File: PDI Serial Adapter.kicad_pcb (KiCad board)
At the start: 2 copper layers, 40 x 17.5 mm, 7 parts, among them J1 2.54, J2 1.27, J3 PROG, J4 FTDI, J5 FTDI_VCC, J6 DTR_RST, J7 TARGET_PWR

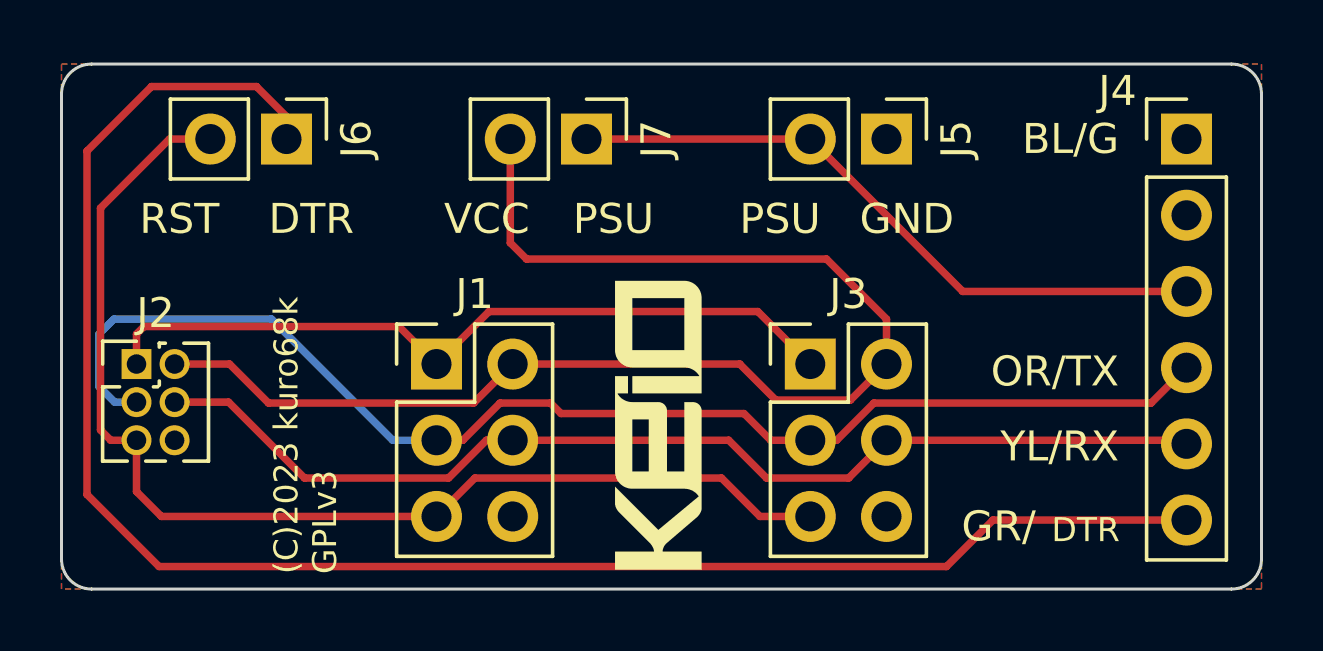
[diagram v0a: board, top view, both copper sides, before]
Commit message: Removed RX/TX from programmer header
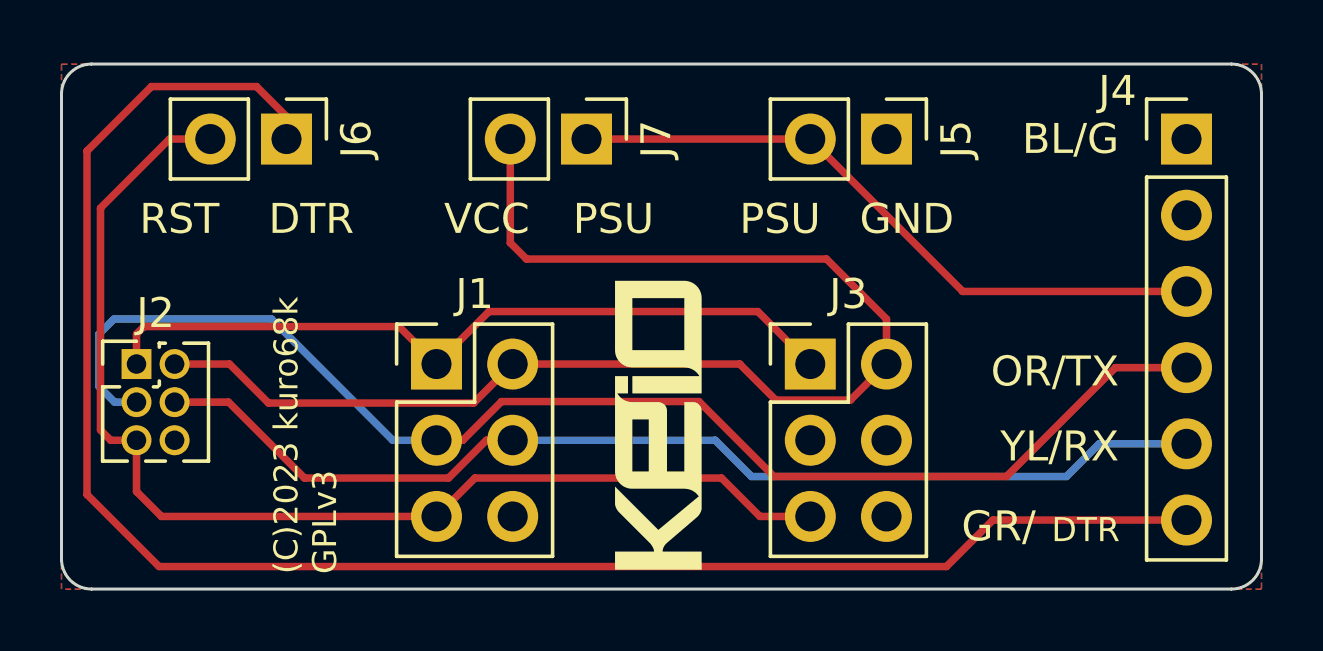
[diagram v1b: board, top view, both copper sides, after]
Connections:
- J3 pad 3: /MCU_RX -> unconnected-(J3-Pin_3-Pad3)
- J3 pad 4: /MCU_TX -> unconnected-(J3-Pin_4-Pad4)
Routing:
- net /MCU_RX: track 43.4 -> 44.4 mm
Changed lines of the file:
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@@
   (net 8 "/FTDI_VCC")
   (net 9 "/DTR")
+  (net 10 "unconnected-(J3-Pin_3-Pad3)")
+  (net 11 "unconnected-(J3-Pin_4-Pad4)")
   (footprint "Connector_PinHeader_2.54mm:PinHeader_2x03_P2.54mm_Vertical" (layer "F.Cu")
     (at 115 52.5)
@@
       (net 2 "/VCC") (pinfunction "Pin_2") (pintype "passive"))
     (pad "3" thru_hole oval (at 0 2.54) (size 1.7 1.7) (drill 1) (layers "*.Cu" "*.Mask")
-      (net 3 "/MCU_RX") (pinfunction "Pin_3") (pintype "passive"))
+      (net 10 "unconnected-(J3-Pin_3-Pad3)") (pinfunction "Pin_3") (pintype "passive+no_connect"))
     (pad "4" thru_hole oval (at 2.54 2.54) (size 1.7 1.7) (drill 1) (layers "*.Cu" "*.Mask")
-      (net 4 "/MCU_TX") (pinfunction "Pin_4") (pintype "passive"))
+      (net 11 "unconnected-(J3-Pin_4-Pad4)") (pinfunction "Pin_4") (pintype "passive+no_connect"))
     (pad "5" thru_hole oval (at 0 5.08) (size 1.7 1.7) (drill 1) (layers "*.Cu" "*.Mask")
       (net 5 "/PDI_CLK") (pinfunction "Pin_5") (pintype "passive"))
@@
   (segment (start 130 51) (end 128 49) (width 0.25) (layer "F.Cu") (net 2))
   (segment (start 128 49) (end 118 49) (width 0.25) (layer "F.Cu") (net 2))
-  (segment (start 127.46 55.04) (end 128.338299 55.04) (width 0.25) (layer "F.Cu") (net 3))
-  (segment (start 128.338299 55.04) (end 129.578299 53.8) (width 0.25) (layer "F.Cu") (net 3))
-  (segment (start 125.25 54.15) (end 126.14 55.04) (width 0.25) (layer "F.Cu") (net 3))
-  (segment (start 119.15 54.15) (end 125.25 54.15) (width 0.25) (layer "F.Cu") (net 3))
-  (segment (start 129.578299 53.8) (end 138.82 53.8) (width 0.25) (layer "F.Cu") (net 3))
-  (segment (start 126.14 55.04) (end 127.46 55.04) (width 0.25) (layer "F.Cu") (net 3))
-  (segment (start 115.878299 55.04) (end 117.118299 53.8) (width 0.25) (layer "F.Cu") (net 3))
   (segment (start 115 55.04) (end 115.878299 55.04) (width 0.25) (layer "F.Cu") (net 3))
-  (segment (start 117.118299 53.8) (end 118.8 53.8) (width 0.25) (layer "F.Cu") (net 3))
-  (segment (start 138.82 53.8) (end 140 52.62) (width 0.25) (layer "F.Cu") (net 3))
-  (segment (start 118.8 53.8) (end 119.15 54.15) (width 0.25) (layer "F.Cu") (net 3))
+  (segment (start 137.63 52.62) (end 140 52.62) (width 0.25) (layer "F.Cu") (net 3))
+  (segment (start 117.168299 53.75) (end 123.75 53.75) (width 0.25) (layer "F.Cu") (net 3))
+  (segment (start 123.75 53.75) (end 126.25 56.25) (width 0.25) (layer "F.Cu") (net 3))
+  (segment (start 126.25 56.25) (end 134 56.25) (width 0.25) (layer "F.Cu") (net 3))
+  (segment (start 134 56.25) (end 137.63 52.62) (width 0.25) (layer "F.Cu") (net 3))
+  (segment (start 115.878299 55.04) (end 117.168299 53.75) (width 0.25) (layer "F.Cu") (net 3))
   (segment (start 109.5 51) (end 113.54 55.04) (width 0.25) (layer "B.Cu") (net 3))
   (segment (start 104.25 51) (end 109.5 51) (width 0.25) (layer "B.Cu") (net 3))
@@
   (segment (start 113.54 55.04) (end 115 55.04) (width 0.25) (layer "B.Cu") (net 3))
   (segment (start 115.401701 56.3) (end 110.6 56.3) (width 0.25) (layer "F.Cu") (net 4))
-  (segment (start 124.74 55.04) (end 126 56.3) (width 0.25) (layer "F.Cu") (net 4))
-  (segment (start 117.54 55.04) (end 124.74 55.04) (width 0.25) (layer "F.Cu") (net 4))
   (segment (start 110.6 56.3) (end 108.07 53.77) (width 0.25) (layer "F.Cu") (net 4))
-  (segment (start 128.74 56.3) (end 130 55.04) (width 0.25) (layer "F.Cu") (net 4))
-  (segment (start 139.88 55.04) (end 140 55.16) (width 0.25) (layer "F.Cu") (net 4))
-  (segment (start 130 55.04) (end 139.88 55.04) (width 0.25) (layer "F.Cu") (net 4))
   (segment (start 117.54 55.04) (end 116.661701 55.04) (width 0.25) (layer "F.Cu") (net 4))
-  (segment (start 126 56.3) (end 128.74 56.3) (width 0.25) (layer "F.Cu") (net 4))
   (segment (start 108.07 53.77) (end 106.27 53.77) (width 0.25) (layer "F.Cu") (net 4))
   (segment (start 116.661701 55.04) (end 115.401701 56.3) (width 0.25) (layer "F.Cu") (net 4))
+  (segment (start 117.54 55.04) (end 124.29 55.04) (width 0.25) (layer "B.Cu") (net 4))
+  (segment (start 137.09 55.16) (end 140 55.16) (width 0.25) (layer "B.Cu") (net 4))
+  (segment (start 124.29 55.04) (end 125.5 56.25) (width 0.25) (layer "B.Cu") (net 4))
+  (segment (start 125.5 56.25) (end 136 56.25) (width 0.25) (layer "B.Cu") (net 4))
+  (segment (start 136 56.25) (end 137.09 55.16) (width 0.25) (layer "B.Cu") (net 4))
   (segment (start 105.83 57.58) (end 105 56.75) (width 0.25) (layer "F.Cu") (net 5))
   (segment (start 103.8 47.3) (end 106.1 45) (width 0.25) (layer "F.Cu") (net 5))

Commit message: Open drain for DTR reset
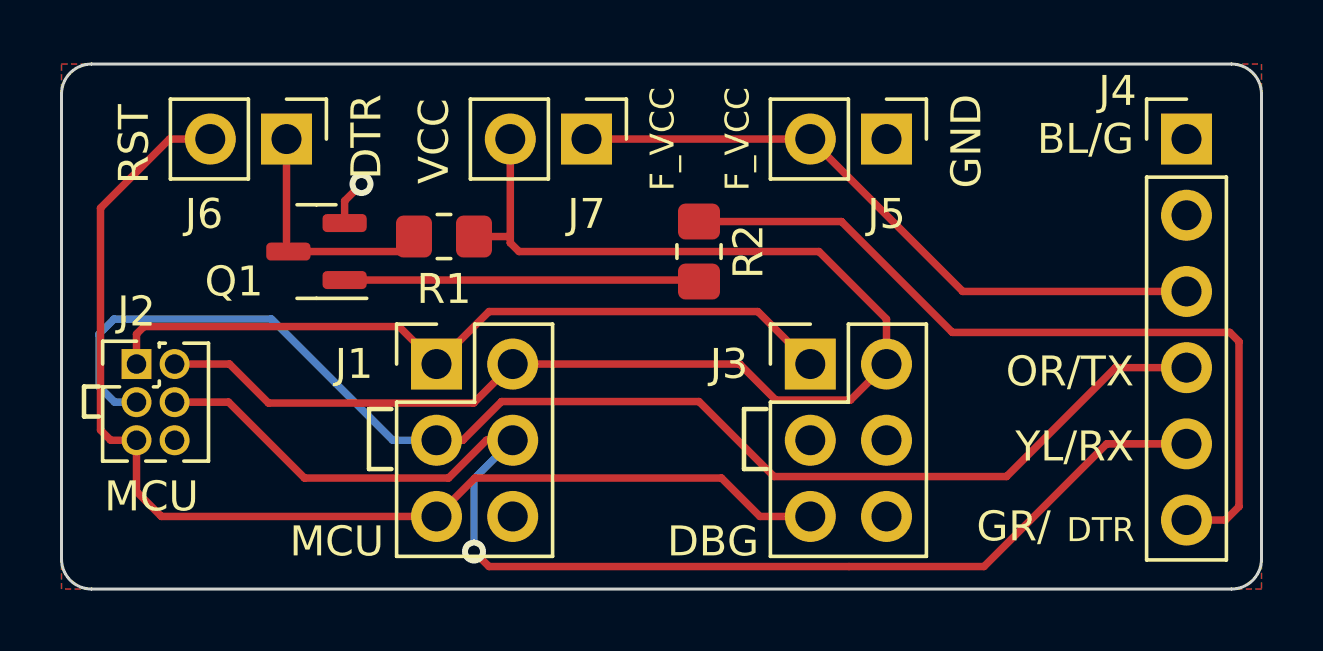
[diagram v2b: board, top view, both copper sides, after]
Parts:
- added Q1: BSS138, Package_TO_SOT_SMD:SOT-23, F.Cu at (111.0, 48.8)
- added R1: 100k, Resistor_SMD:R_0805_2012Metric_Pad1.20x1.40mm_HandSolder, F.Cu at (115.2, 48.2)
- added R2: 1k, Resistor_SMD:R_0805_2012Metric_Pad1.20x1.40mm_HandSolder, F.Cu at (123.8, 48.8)
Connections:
- J6 pad 1: /DTR -> Net-(J6-Pin_1)
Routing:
- net /DTR: track 58.4 -> 27.1 mm
- net Net-(Q1-G): track 0.00 -> 11.8 mm
- net Net-(J6-Pin_1): track 0.00 -> 8.17 mm
- net /MCU_TX: track 36.3 -> 42.7 mm, vias 0 -> 1
- net /GND: track 0.00 -> 1.53 mm, vias 0 -> 1
- net /VCC: track 44.4 -> 45.6 mm
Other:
- board text added: "DBG"
- board text added: "F_VCC"
- board text added: "MCU"
- board text removed: "PSU"

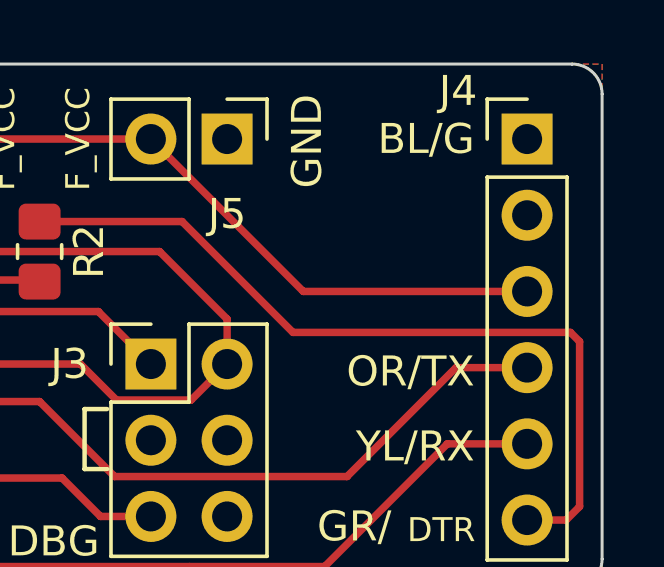
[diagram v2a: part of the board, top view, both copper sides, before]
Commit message: Added FTDI to silkscreen
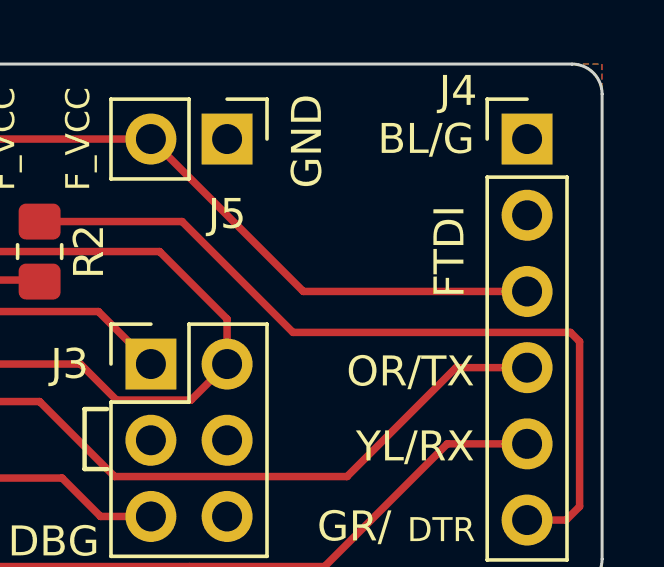
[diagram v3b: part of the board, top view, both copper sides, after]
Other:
- board text added: "FTDI"
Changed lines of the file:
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@@
     (effects (font (size 1 1) (thickness 0.15)) (justify left bottom))
+  )
+  (gr_text "FTDI" (at 138 48.75 90) (layer "F.SilkS")
+    (effects (font (size 1 1) (thickness 0.15)) (justify bottom))
   )
   (gr_text "RST" (at 105.5 46.5 90) (layer "F.SilkS")

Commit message: Fabrication settings
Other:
- board text added: "(C)2023 kuro68k GPLv3 Rev 1"
- board text removed: "(C)2023 kuro68k GPLv3"
